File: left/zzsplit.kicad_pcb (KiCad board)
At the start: 2 copper layers, 160.9 x 98.9 mm, 77 parts, among them J1 OLED, J2 MJ-4PP-9-Lily58-cache, J3 Conn_01x02_Female, SW1 SW_PUSH-MX_W_LED, SW10 SW_PUSH-MX_W_LED, SW11 SW_PUSH-MX_W_LED, SW12 SW_PUSH-MX_W_LED, SW13 SW_PUSH-MX_W_LED, SW14 SW_PUSH-MX_W_LED, SW15 SW_PUSH-MX_W_LED, SW16 SW_PUSH-MX_W_LED, SW17 SW_PUSH-MX_W_LED, SW18 SW_PUSH-MX_W_LED, SW19 SW_PUSH-MX_W_LED, SW2 SW_PUSH-MX_W_LED, SW20 SW_PUSH-MX_W_LED, SW21 SW_PUSH-MX_W_LED, SW22 SW_PUSH-MX_W_LED, SW23 SW_PUSH-MX_W_LED, SW24 SW_PUSH-MX_W_LED, SW25 SW_PUSH-MX_W_LED, SW26 SW_PUSH-MX_W_LED, SW27 SW_PUSH-MX_W_LED, SW28 SW_PUSH-MX_W_LED, SW29 SW_PUSH-MX_W_LED, SW3 SW_PUSH-MX_W_LED, SW30 SW_PUSH-MX_W_LED, SW31 SW_SPDT, SW32 SW_Push, SW4 SW_PUSH-MX_W_LED, SW5 SW_PUSH-MX_W_LED, SW6 SW_PUSH-MX_W_LED, SW7 SW_PUSH-MX_W_LED, SW8 SW_PUSH-MX_W_LED, SW9 SW_PUSH-MX_W_LED, U1 ProMicro

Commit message: pcb fixup && new gerber
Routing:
- net GND: track 215.4 -> 290.3 mm, vias 51 -> 83
- net Net-(D20-Pad2): track 29.3 -> 32.9 mm
- net Net-(D18-Pad2): track 29.5 -> 28.8 mm

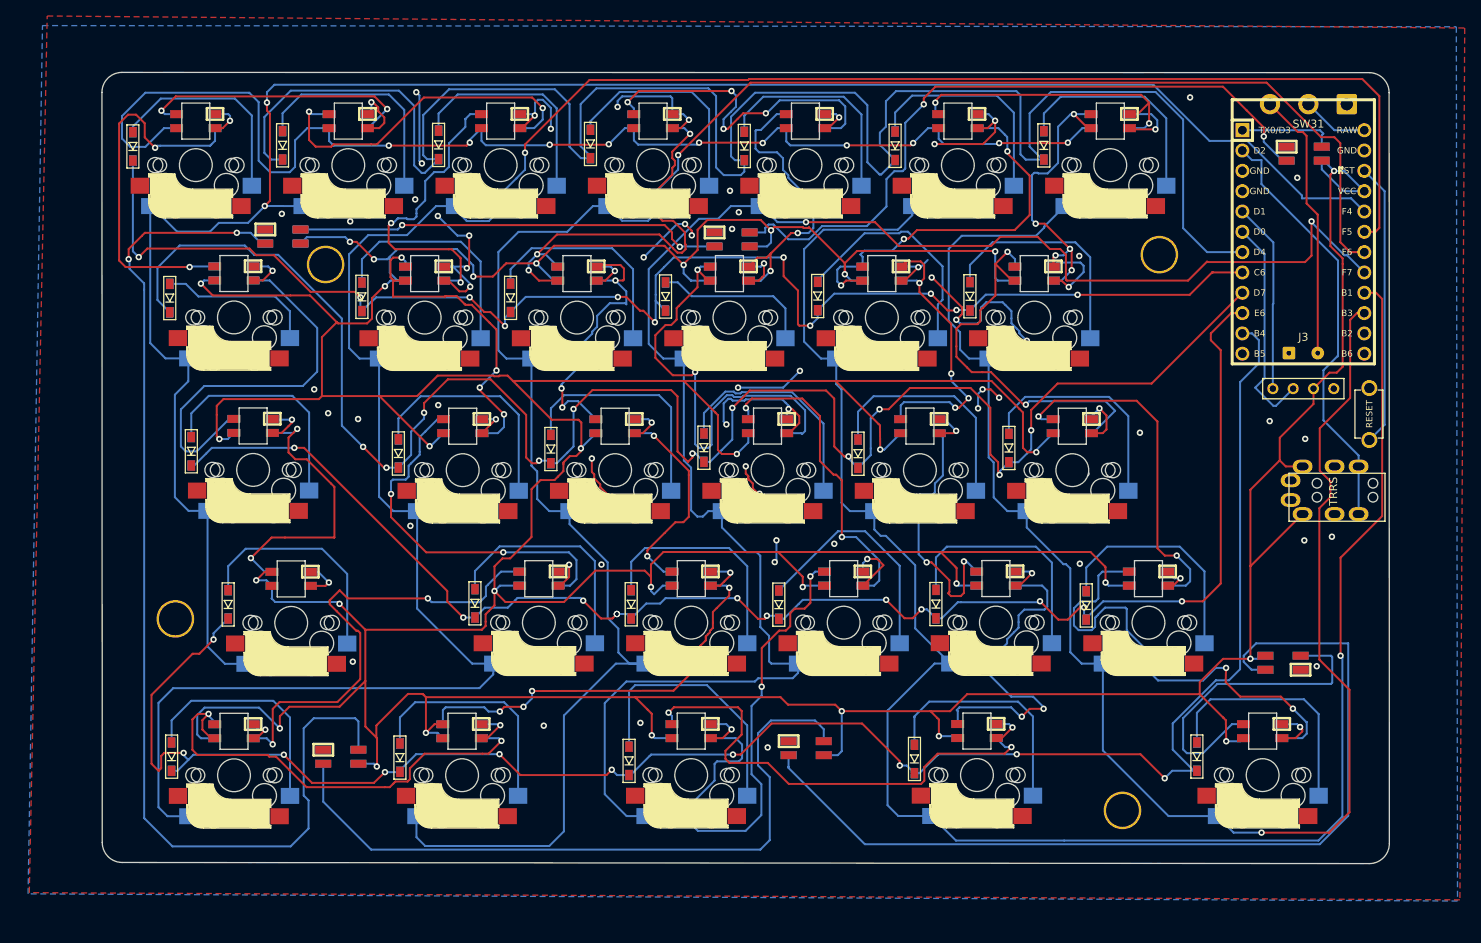
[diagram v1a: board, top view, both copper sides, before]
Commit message: fix rgb powerline problem and new 3 pin 2 channel switches
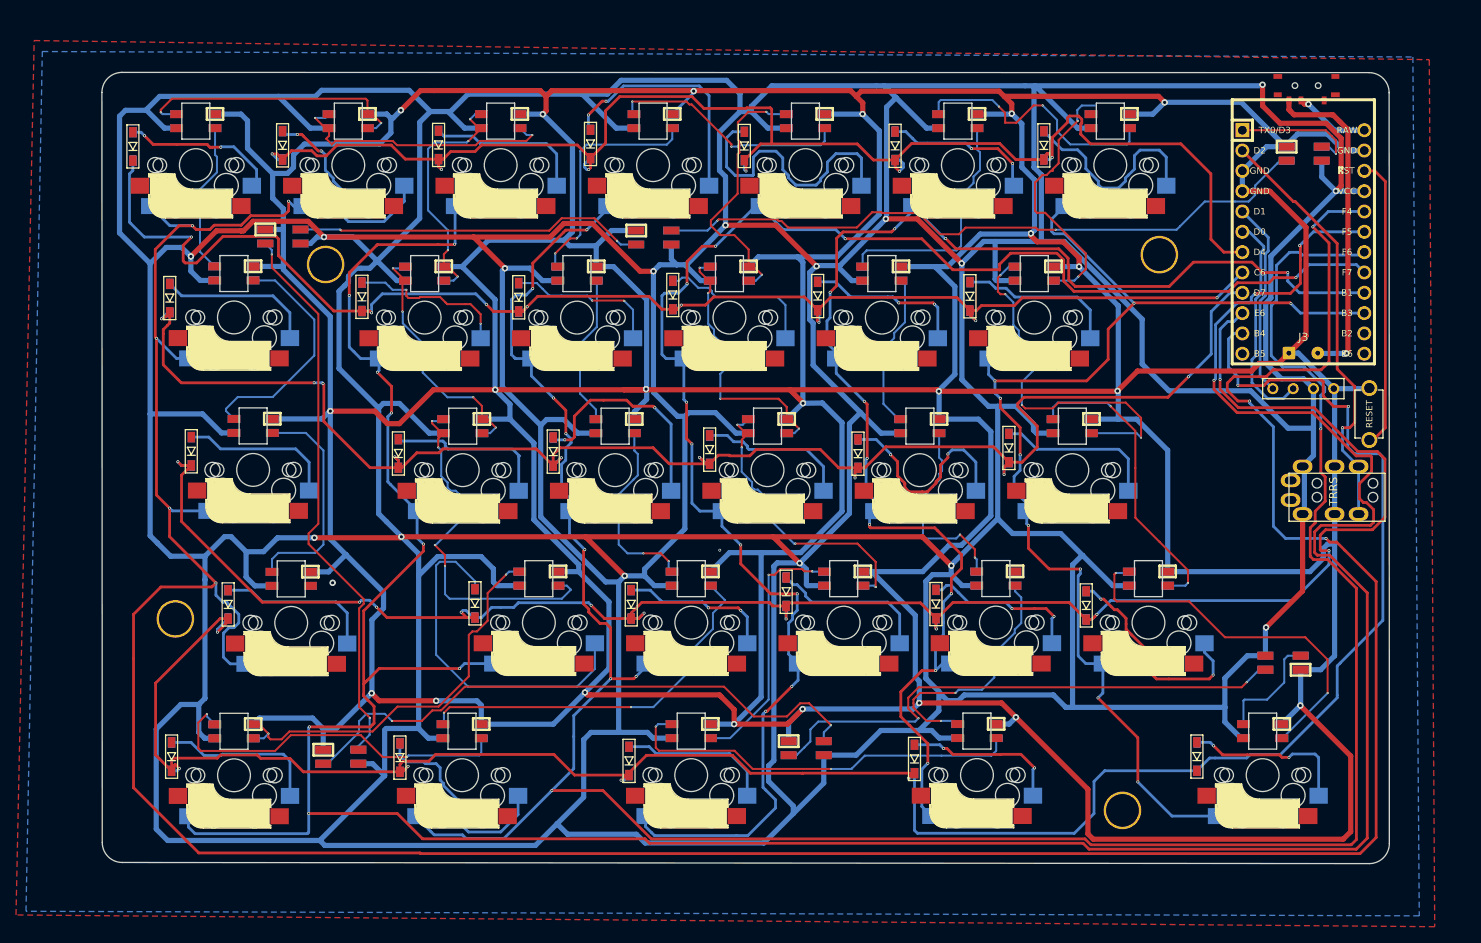
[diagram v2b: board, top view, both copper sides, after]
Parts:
- SW31: footprint Connector_Wire:SolderWire-0.75sqmm_1x03_P4.8mm_D1.25mm_OD2.3mm -> switch:switch-MSK-12C02-smd
- moved D32 9.79 mm to (124.7, 64.1)
- moved SW31 6.23 mm to (206.3, 43.8), turned to -90 degrees
- moved D19 1.85 mm to (141.2, 108.4)
- moved D12 1.02 mm to (107.8, 71.6)
- moved D17 0.93 mm to (127.1, 71.3)
- moved D18 0.76 mm to (131.7, 90.6)
- moved D13 0.43 mm to (112.1, 90.9)
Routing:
- net GND: track 290.3 -> 1146.0 mm, vias 83 -> 24
- net VDD: track 992.0 -> 1481.9 mm, vias 42 -> 16
- net Col1: track 248.8 -> 399.1 mm, vias 2 -> 8
- net Col2: track 287.3 -> 393.0 mm, vias 1 -> 11
- net Net-(D33-Pad1): track 137.2 -> 70.8 mm
- net Row1: track 240.5 -> 176.4 mm, vias 0 -> 6
- net Col3: track 250.5 -> 313.8 mm, vias 1 -> 9
- net Col5: track 230.6 -> 170.8 mm, vias 1 -> 10
- net Row4: track 189.9 -> 240.3 mm, vias 12 -> 11
- net Net-(D35-Pad1): track 116.2 -> 68.3 mm, vias 0 -> 2
- net Col6: track 196.1 -> 148.7 mm, vias 1 -> 9
- net Row3: track 235.0 -> 194.8 mm, vias 11 -> 9
- net Row5: track 235.3 -> 275.5 mm, vias 10 -> 7
- net Net-(SW22-Pad3): track 64.7 -> 32.3 mm
- net Net-(SW13-Pad3): track 46.6 -> 19.0 mm, vias 2 -> 0
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
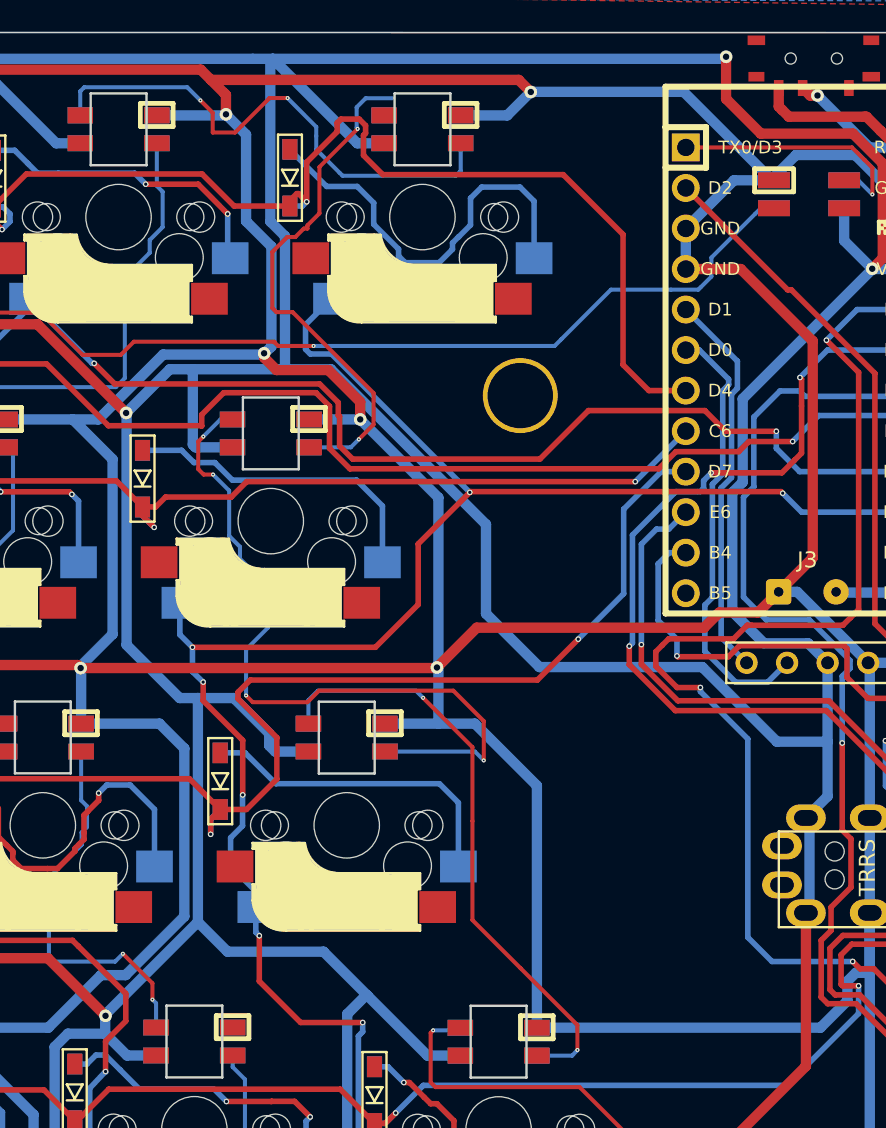
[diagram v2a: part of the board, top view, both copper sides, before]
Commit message: new top & bottom plates
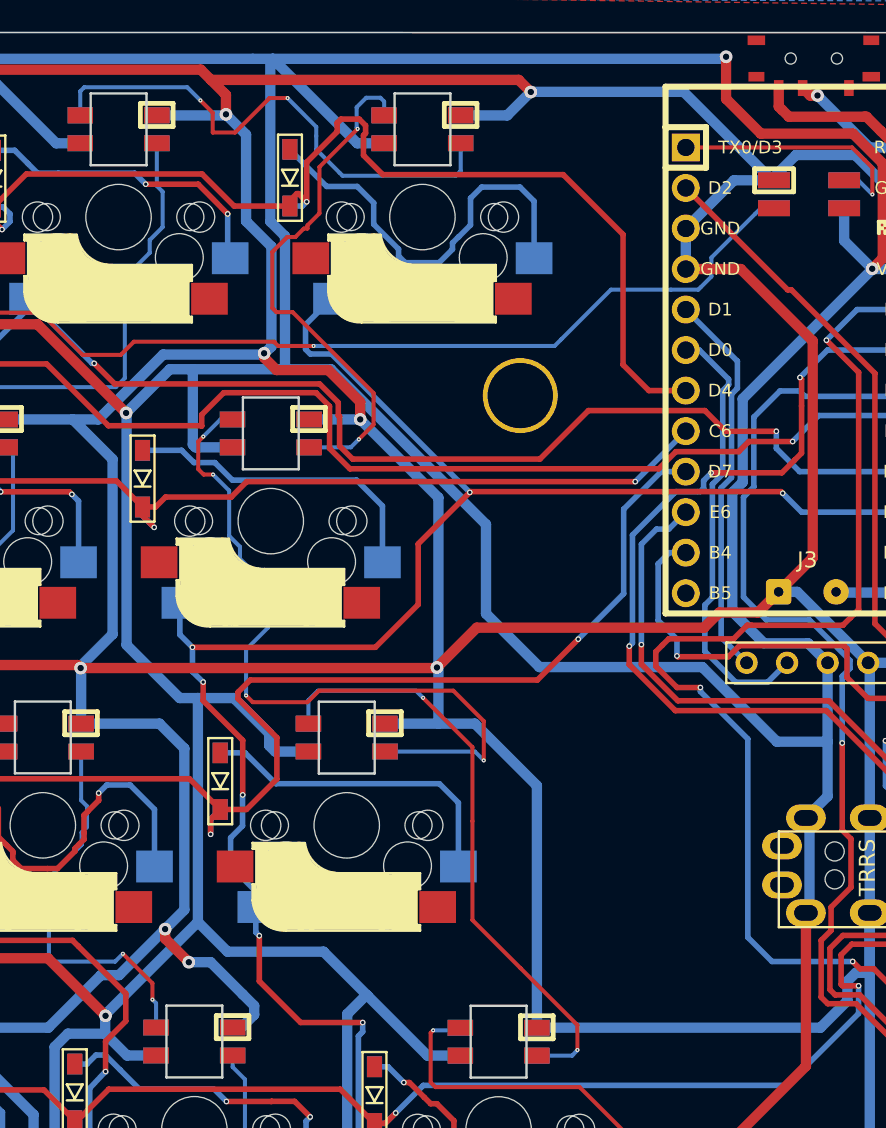
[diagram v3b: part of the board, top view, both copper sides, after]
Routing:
- net GND: track 1146.0 -> 1156.0 mm, vias 24 -> 26
